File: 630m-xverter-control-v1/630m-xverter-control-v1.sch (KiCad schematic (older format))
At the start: 49 parts, among them J1 Rig Transverter, J2 ALC, J3 ANT, J4 TX_TO_AMP, J5 TX_FROM_AMP, J6 Power, J7 TX AMP POWER, K1 DS1E-M-DC12V, K2 DS1E-M-DC12V, K3 DS1E-M-DC12V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

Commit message: Updates!
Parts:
- added H1, H2, H3, H4: GND, MountingHole:MountingHole_4.3x6.2mm_M4_Pad_Via, symbol Mechanical:MountingHole_Pad
- C1, C2: footprint (none) -> Capacitor_THT:C_Rect_L10.3mm_W5.7mm_P7.50mm_MKS4
- C3: renamed from C1; footprint (none) -> Capacitor_THT:C_Disc_D5.0mm_W2.5mm_P5.00mm
- C4: renamed from C2; footprint (none) -> Capacitor_THT:C_Disc_D5.0mm_W2.5mm_P5.00mm
- C5: renamed from C3; footprint (none) -> Capacitor_THT:C_Disc_D5.0mm_W2.5mm_P5.00mm
- C6: renamed from C4; footprint (none) -> Capacitor_THT:C_Disc_D5.0mm_W2.5mm_P5.00mm
- C7: footprint (none) -> Capacitor_THT:CP_Radial_D10.0mm_P2.50mm
- C8: renamed from C5; footprint (none) -> Capacitor_THT:C_Disc_D5.0mm_W2.5mm_P5.00mm
- C9: renamed from C6; footprint (none) -> Capacitor_THT:CP_Radial_D10.0mm_P2.50mm
- D1, D2: footprint (none) -> Diode_THT:D_DO-35_SOD27_P10.16mm_Horizontal
- D3, D4, D5, D6, D7: footprint (none) -> Diode_THT:D_DO-41_SOD81_P10.16mm_Horizontal
- J1: footprint (none) -> Connector_PinHeader_2.54mm:PinHeader_1x08_P2.54mm_Vertical
- J2, J6, J7: footprint (none) -> Connector_PinHeader_2.54mm:PinHeader_1x02_P2.54mm_Vertical
- J3, J4, J5: footprint (none) -> Connector_Coaxial:SMA_Amphenol_132134-11_Vertical
- K1, K2, K3: footprint Panasonic-DS1E-M-DC12V-0-0-* -> Package_DIP:DIP-12_W7.62mm
- L1, L2, L3: footprint (none) -> coilcraft:coilcraft_slot10
- R1, R10, R2, R3, R4, R5, R6, R7, R8, R9: footprint (none) -> Resistor_THT:R_Axial_DIN0207_L6.3mm_D2.5mm_P7.62mm_Horizontal
- R11: renamed from R9; footprint (none) -> Resistor_THT:R_Axial_DIN0207_L6.3mm_D2.5mm_P7.62mm_Horizontal
- R12: renamed from R10; footprint (none) -> Resistor_THT:R_Axial_DIN0207_L6.3mm_D2.5mm_P7.62mm_Horizontal
- R13: renamed from R11; footprint (none) -> Resistor_THT:R_Axial_DIN0207_L6.3mm_D2.5mm_P10.16mm_Horizontal
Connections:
- net XVERTER_TX_OUTPUT is gone; now on net TX_TO_AMP: J1.7 (Pin_7)
- net GND: now also H1.1, H2.1, H3.1, H4.1

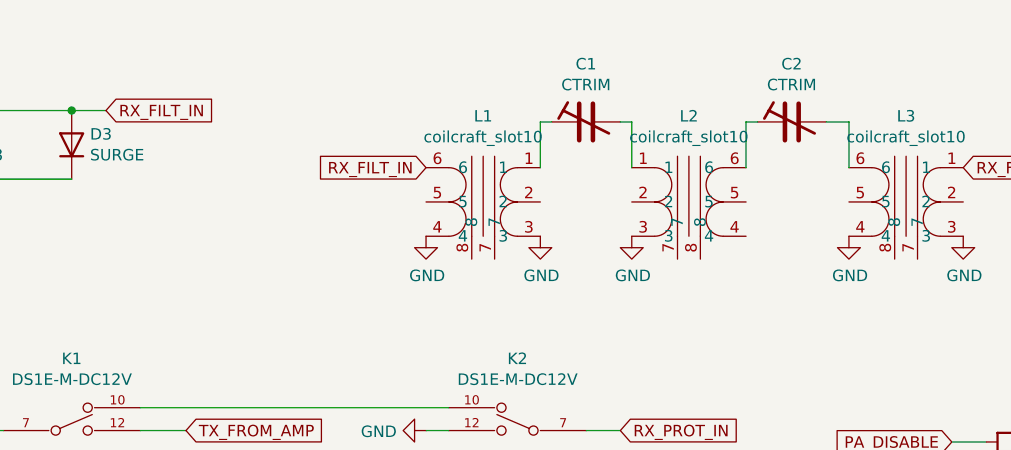
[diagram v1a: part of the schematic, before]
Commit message: Whoops - my coil orientation/pinout was JUST PLAIN WRONG.
So fix the schematic to do the right thing; I'll have to hack something on my
development pcb to test that the filter actually works..
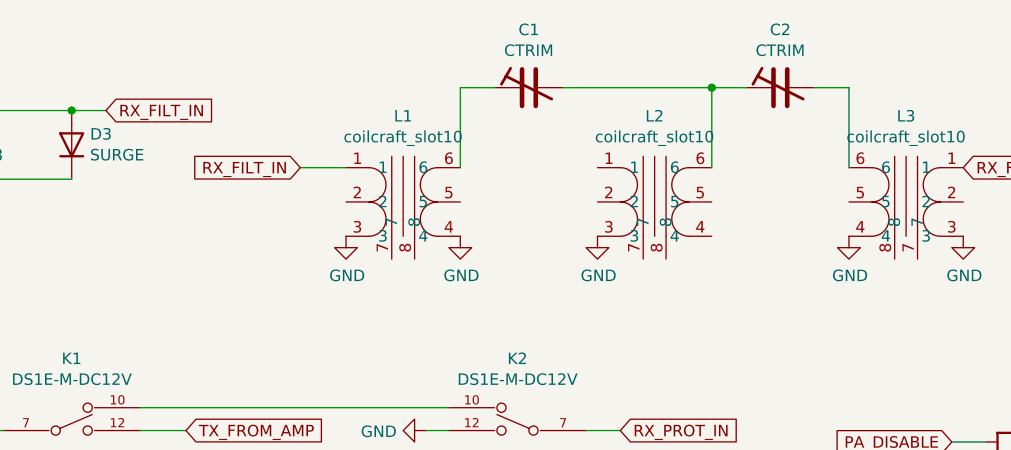
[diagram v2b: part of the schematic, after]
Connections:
- net RX_FILT_IN: now also L1.1; no longer L1.6
- net at C1.1: now also L1.6; no longer L1.1
- net at L2.1: no longer C1.2
- net at C2.1, L2.6: now also C1.2
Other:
- moved on the sheet: C1, C2, L1, L2
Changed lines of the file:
@@
 TX_ENABLE
-$Comp
-L coilcraft:coilcraft_slot10 L1
-U 1 1 5FA3D136
-P 6050 1150
-F 0 "L1" H 6050 1375 50  0000 C CNN
-F 1 "coilcraft_slot10" H 6050 1284 50  0000 C CNN
-F 2 "coilcraft:coilcraft_slot10" H 6050 1150 50  0001 C CNN
-F 3 "" H 6050 1150 50  0001 C CNN
-	1    6050 1150
-	-1   0    0    -1
-$EndComp
 $Comp
 L coilcraft:coilcraft_slot10 L2
 U 1 1 5FA3E025
-P 6950 1150
-F 0 "L2" H 6950 1375 50  0000 C CNN
-F 1 "coilcraft_slot10" H 6950 1284 50  0000 C CNN
-F 2 "coilcraft:coilcraft_slot10" H 6950 1150 50  0001 C CNN
-F 3 "" H 6950 1150 50  0001 C CNN
-	1    6950 1150
+P 6800 1150
+F 0 "L2" H 6800 1375 50  0000 C CNN
+F 1 "coilcraft_slot10" H 6800 1284 50  0000 C CNN
+F 2 "coilcraft:coilcraft_slot10" H 6800 1150 50  0001 C CNN
+F 3 "" H 6800 1150 50  0001 C CNN
+	1    6800 1150
 	1    0    0    -1
 $EndComp
@@
 L power:GND #PWR0103
 U 1 1 5FA420D7
-P 5800 1450
-F 0 "#PWR0103" H 5800 1200 50  0001 C CNN
-F 1 "GND" H 5805 1277 50  0000 C CNN
-F 2 "" H 5800 1450 50  0001 C CNN
-F 3 "" H 5800 1450 50  0001 C CNN
-	1    5800 1450
+P 5450 1450
+F 0 "#PWR0103" H 5450 1200 50  0001 C CNN
+F 1 "GND" H 5455 1277 50  0000 C CNN
+F 2 "" H 5450 1450 50  0001 C CNN
+F 3 "" H 5450 1450 50  0001 C CNN
+	1    5450 1450
 	1    0    0    -1
 $EndComp
@@
 L power:GND #PWR0104
 U 1 1 5FA42988
-P 6300 1450
-F 0 "#PWR0104" H 6300 1200 50  0001 C CNN
-F 1 "GND" H 6305 1277 50  0000 C CNN
-F 2 "" H 6300 1450 50  0001 C CNN
-F 3 "" H 6300 1450 50  0001 C CNN
-	1    6300 1450
+P 5950 1450
+F 0 "#PWR0104" H 5950 1200 50  0001 C CNN
+F 1 "GND" H 5955 1277 50  0000 C CNN
+F 2 "" H 5950 1450 50  0001 C CNN
+F 3 "" H 5950 1450 50  0001 C CNN
+	1    5950 1450
 	1    0    0    -1
 $EndComp
@@
 L power:GND #PWR0105
 U 1 1 5FA47F16
-P 6700 1450
-F 0 "#PWR0105" H 6700 1200 50  0001 C CNN
-F 1 "GND" H 6705 1277 50  0000 C CNN
-F 2 "" H 6700 1450 50  0001 C CNN
-F 3 "" H 6700 1450 50  0001 C CNN
-	1    6700 1450
+P 6550 1450
+F 0 "#PWR0105" H 6550 1200 50  0001 C CNN
+F 1 "GND" H 6555 1277 50  0000 C CNN
+F 2 "" H 6550 1450 50  0001 C CNN
+F 3 "" H 6550 1450 50  0001 C CNN
+	1    6550 1450
 	1    0    0    -1
 $EndComp
@@
 L Device:CTRIM C1
 U 1 1 5FA4943F
-P 6500 950
-F 0 "C1" V 6753 950 50  0000 C CNN
-F 1 "CTRIM" V 6662 950 50  0000 C CNN
-F 2 "Capacitor_THT:C_Rect_L10.3mm_W5.7mm_P7.50mm_MKS4" H 6500 950 50  0001 C CNN
-F 3 "~" H 6500 950 50  0001 C CNN
-	1    6500 950
+P 6250 800
+F 0 "C1" V 6503 800 50  0000 C CNN
+F 1 "CTRIM" V 6412 800 50  0000 C CNN
+F 2 "Capacitor_THT:C_Rect_L10.3mm_W5.7mm_P7.50mm_MKS4" H 6250 800 50  0001 C CNN
+F 3 "~" H 6250 800 50  0001 C CNN
+	1    6250 800
 	0    -1   -1   0
 $EndComp
@@
 L Device:CTRIM C2
 U 1 1 5FA50CBE
-P 7400 950
-F 0 "C2" V 7653 950 50  0000 C CNN
-F 1 "CTRIM" V 7562 950 50  0000 C CNN
-F 2 "Capacitor_THT:C_Rect_L10.3mm_W5.7mm_P7.50mm_MKS4" H 7400 950 50  0001 C CNN
-F 3 "~" H 7400 950 50  0001 C CNN
-	1    7400 950
+P 7350 800
+F 0 "C2" V 7603 800 50  0000 C CNN
+F 1 "CTRIM" V 7512 800 50  0000 C CNN
+F 2 "Capacitor_THT:C_Rect_L10.3mm_W5.7mm_P7.50mm_MKS4" H 7350 800 50  0001 C CNN
+F 3 "~" H 7350 800 50  0001 C CNN
+	1    7350 800
 	0    -1   -1   0
 $EndComp
-Wire Wire Line
-	6350 950  6300 950
-Wire Wire Line
-	6300 950  6300 1150
-Wire Wire Line
-	6650 950  6700 950
-Wire Wire Line
-	6700 950  6700 1150
-Wire Wire Line
-	7250 950  7200 950
-Wire Wire Line
-	7200 950  7200 1150
-Wire Wire Line
-	7550 950  7650 950
-Wire Wire Line
-	7650 950  7650 1150
-Text GLabel 5800 1150 0    50   Input ~ 0
+Text GLabel 5250 1150 0    50   Input ~ 0
 RX_FILT_IN
 Text GLabel 8150 1150 2    50   Input ~ 0
@@
 Wire Wire Line
 	8200 3200 8100 3200
+$Comp
+L coilcraft:coilcraft_slot10 L1
+U 1 1 5FA3D136
+P 5700 1150
+F 0 "L1" H 5700 1375 50  0000 C CNN
+F 1 "coilcraft_slot10" H 5700 1284 50  0000 C CNN
+F 2 "coilcraft:coilcraft_slot10" H 5700 1150 50  0001 C CNN
+F 3 "" H 5700 1150 50  0001 C CNN
+	1    5700 1150
+	1    0    0    -1
+$EndComp
+Wire Wire Line
+	5450 1150 5250 1150
+Wire Wire Line
+	5950 1150 5950 800
+Wire Wire Line
+	5950 800  6100 800
+Wire Wire Line
+	7500 800  7650 800
+Wire Wire Line
+	7650 800  7650 1150
+Wire Wire Line
+	6400 800  7050 800
+Wire Wire Line
+	7050 1150 7050 800
+Connection ~ 7050 800
+Wire Wire Line
+	7050 800  7200 800
 $EndSCHEMATC

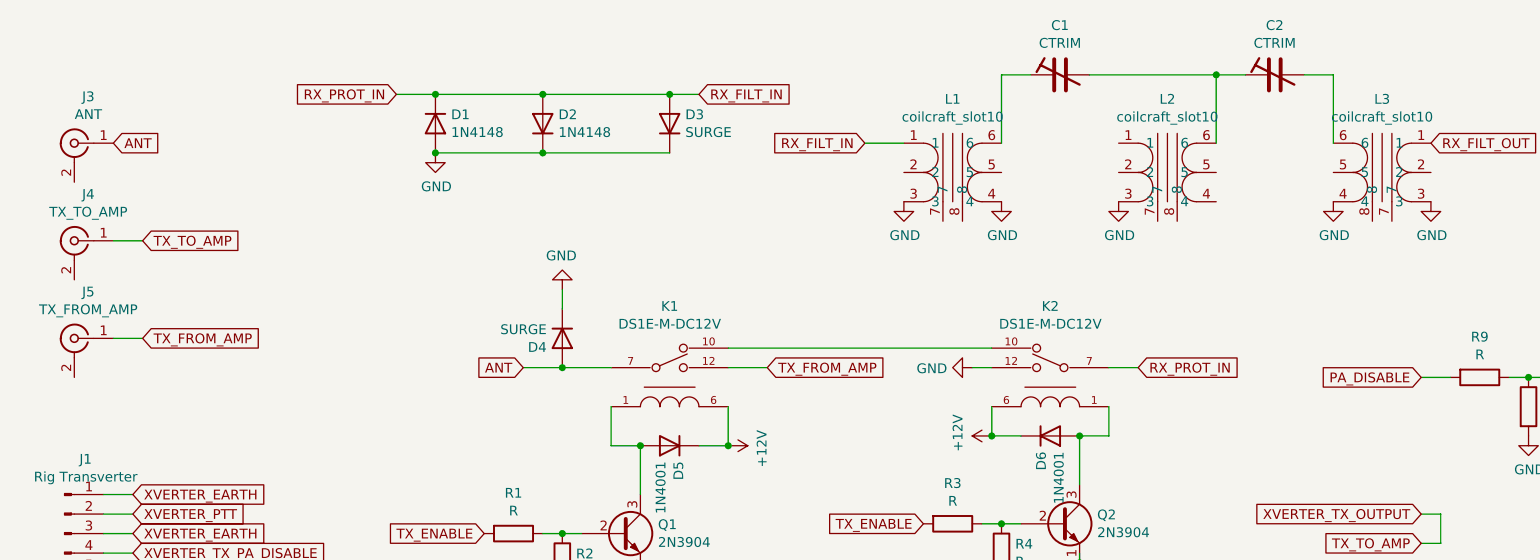
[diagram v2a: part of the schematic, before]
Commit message: more fixes:
* missed ground plane ties for the signal connectors, whoops
* add ground pins for the coils so they can be tied to ground
* add label
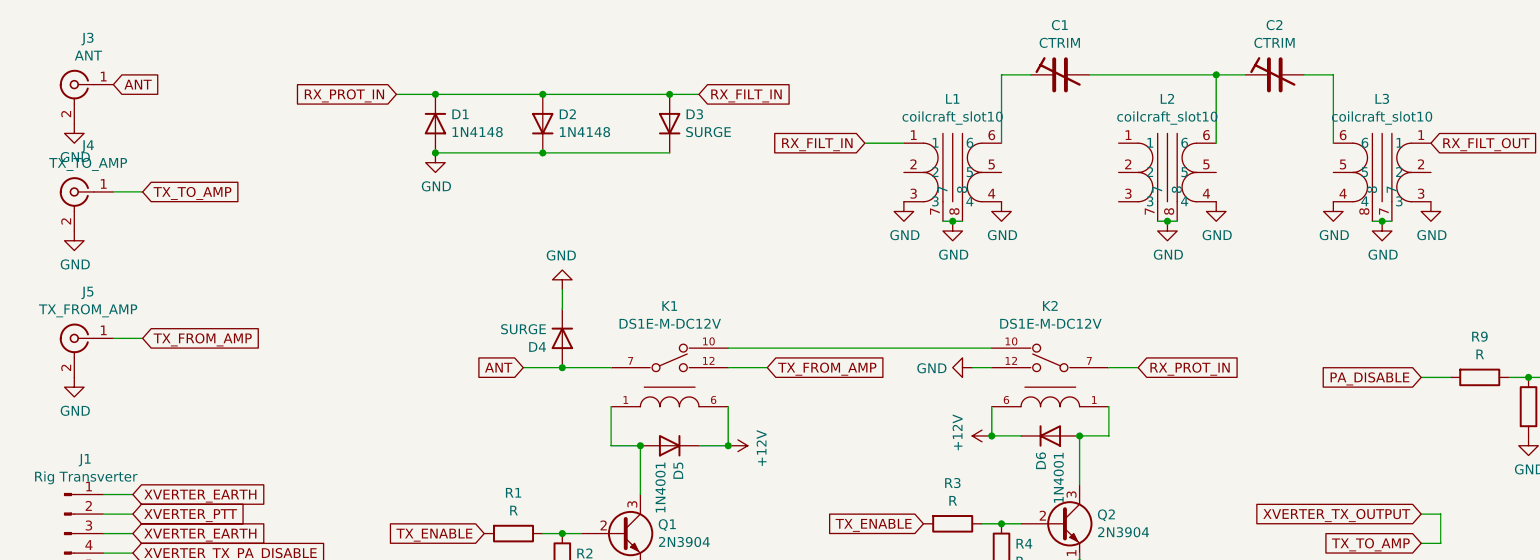
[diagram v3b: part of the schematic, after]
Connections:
- net GND: now also J3.2 (Ext), J4.2 (Ext), J5.2 (Ext), L1.7, L1.8, L2.4, L2.7, L2.8, L3.7, L3.8; no longer L2.3
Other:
- moved on the sheet: J3, J4
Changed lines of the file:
@@
 L power:GND #PWR0105
 U 1 1 5FA47F16
-P 6550 1450
-F 0 "#PWR0105" H 6550 1200 50  0001 C CNN
-F 1 "GND" H 6555 1277 50  0000 C CNN
-F 2 "" H 6550 1450 50  0001 C CNN
-F 3 "" H 6550 1450 50  0001 C CNN
-	1    6550 1450
+P 7050 1450
+F 0 "#PWR0105" H 7050 1200 50  0001 C CNN
+F 1 "GND" H 7055 1277 50  0000 C CNN
+F 2 "" H 7050 1450 50  0001 C CNN
+F 3 "" H 7050 1450 50  0001 C CNN
+	1    7050 1450
 	1    0    0    -1
 $EndComp
@@
 L Connector:Conn_Coaxial J3
 U 1 1 5FA5CD9A
-P 1200 1150
-F 0 "J3" H 1128 1388 50  0000 C CNN
-F 1 "ANT" H 1128 1297 50  0000 C CNN
-F 2 "Connector_Coaxial:SMA_Amphenol_132134-11_Vertical" H 1200 1150 50  0001 C CNN
-F 3 " ~" H 1200 1150 50  0001 C CNN
-	1    1200 1150
+P 1200 850
+F 0 "J3" H 1128 1088 50  0000 C CNN
+F 1 "ANT" H 1128 997 50  0000 C CNN
+F 2 "Connector_Coaxial:SMA_Amphenol_132134-11_Vertical" H 1200 850 50  0001 C CNN
+F 3 " ~" H 1200 850 50  0001 C CNN
+	1    1200 850
 	-1   0    0    -1
 $EndComp
@@
 L Connector:Conn_Coaxial J4
 U 1 1 5FA62FA9
-P 1200 1650
-F 0 "J4" H 1128 1888 50  0000 C CNN
-F 1 "TX_TO_AMP" H 1128 1797 50  0000 C CNN
-F 2 "Connector_Coaxial:SMA_Amphenol_132134-11_Vertical" H 1200 1650 50  0001 C CNN
-F 3 " ~" H 1200 1650 50  0001 C CNN
-	1    1200 1650
+P 1200 1400
+F 0 "J4" H 1128 1638 50  0000 C CNN
+F 1 "TX_TO_AMP" H 1128 1547 50  0000 C CNN
+F 2 "Connector_Coaxial:SMA_Amphenol_132134-11_Vertical" H 1200 1400 50  0001 C CNN
+F 3 " ~" H 1200 1400 50  0001 C CNN
+	1    1200 1400
 	-1   0    0    -1
 $EndComp
@@
 	4400 900  4250 900
 Connection ~ 4250 900
-Text GLabel 1400 1150 2    50   Input ~ 0
+Text GLabel 1400 850  2    50   Input ~ 0
 ANT
 Text GLabel 1500 2950 2    50   Input ~ 0
@@
 Wire Wire Line
 	1350 3650 1500 3650
-Text GLabel 1550 1650 2    50   Input ~ 0
+Text GLabel 1550 1400 2    50   Input ~ 0
 TX_TO_AMP
 Text GLabel 1550 2150 2    50   Input ~ 0
 TX_FROM_AMP
 Wire Wire Line
-	1550 1650 1400 1650
+	1550 1400 1400 1400
 Wire Wire Line
 	1550 2150 1400 2150
@@
 Wire Wire Line
 	7050 800  7200 800
+$Comp
+L power:GND #PWR?
+U 1 1 5FEED7B2
+P 1200 1050
+F 0 "#PWR?" H 1200 800 50  0001 C CNN
+F 1 "GND" H 1205 877 50  0000 C CNN
+F 2 "" H 1200 1050 50  0001 C CNN
+F 3 "" H 1200 1050 50  0001 C CNN
+	1    1200 1050
+	1    0    0    -1
+$EndComp
+$Comp
+L power:GND #PWR?
+U 1 1 5FEF2BFC
+P 1200 1600
+F 0 "#PWR?" H 1200 1350 50  0001 C CNN
+F 1 "GND" H 1205 1427 50  0000 C CNN
+F 2 "" H 1200 1600 50  0001 C CNN
+F 3 "" H 1200 1600 50  0001 C CNN
+	1    1200 1600
+	1    0    0    -1
+$EndComp
+$Comp
+L power:GND #PWR?
+U 1 1 5FEF3573
+P 1200 2350
+F 0 "#PWR?" H 1200 2100 50  0001 C CNN
+F 1 "GND" H 1205 2177 50  0000 C CNN
+F 2 "" H 1200 2350 50  0001 C CNN
+F 3 "" H 1200 2350 50  0001 C CNN
+	1    1200 2350
+	1    0    0    -1
+$EndComp
+Wire Wire Line
+	7850 1550 7900 1550
+Wire Wire Line
+	6750 1550 6800 1550
+Wire Wire Line
+	5650 1550 5700 1550
+$Comp
+L power:GND #PWR?
+U 1 1 5FF0781A
+P 5700 1550
+F 0 "#PWR?" H 5700 1300 50  0001 C CNN
+F 1 "GND" H 5705 1377 50  0000 C CNN
+F 2 "" H 5700 1550 50  0001 C CNN
+F 3 "" H 5700 1550 50  0001 C CNN
+	1    5700 1550
+	1    0    0    -1
+$EndComp
+Connection ~ 5700 1550
+Wire Wire Line
+	5700 1550 5750 1550
+$Comp
+L power:GND #PWR?
+U 1 1 5FF07F9B
+P 6800 1550
+F 0 "#PWR?" H 6800 1300 50  0001 C CNN
+F 1 "GND" H 6805 1377 50  0000 C CNN
+F 2 "" H 6800 1550 50  0001 C CNN
+F 3 "" H 6800 1550 50  0001 C CNN
+	1    6800 1550
+	1    0    0    -1
+$EndComp
+Connection ~ 6800 1550
+Wire Wire Line
+	6800 1550 6850 1550
+$Comp
+L power:GND #PWR?
+U 1 1 5FF08852
+P 7900 1550
+F 0 "#PWR?" H 7900 1300 50  0001 C CNN
+F 1 "GND" H 7905 1377 50  0000 C CNN
+F 2 "" H 7900 1550 50  0001 C CNN
+F 3 "" H 7900 1550 50  0001 C CNN
+	1    7900 1550
+	1    0    0    -1
+$EndComp
+Connection ~ 7900 1550
+Wire Wire Line
+	7900 1550 7950 1550
 $EndSCHEMATC

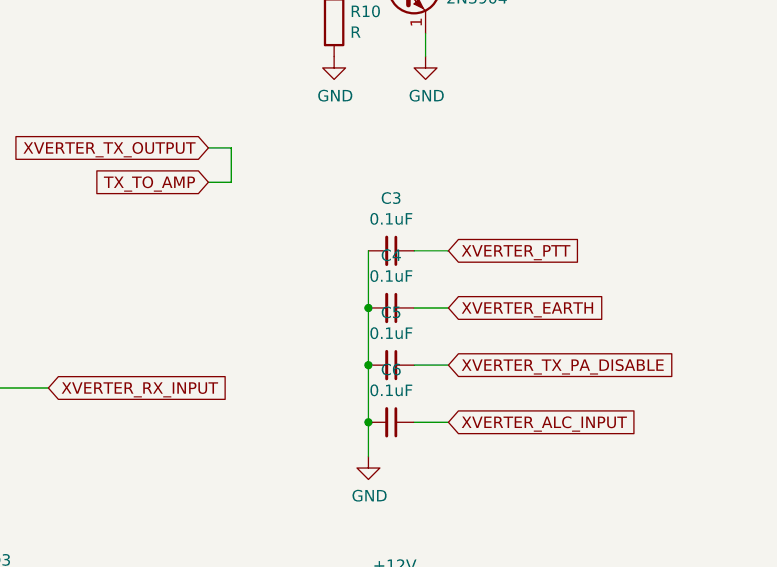
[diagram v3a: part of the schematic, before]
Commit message: More v0.3 fixes -
* fix the bloody signal routing for that middle IF coil, what was I thinking
* don't use a cap to xverter-gnd; just tie them together and to ground

That should be much better!
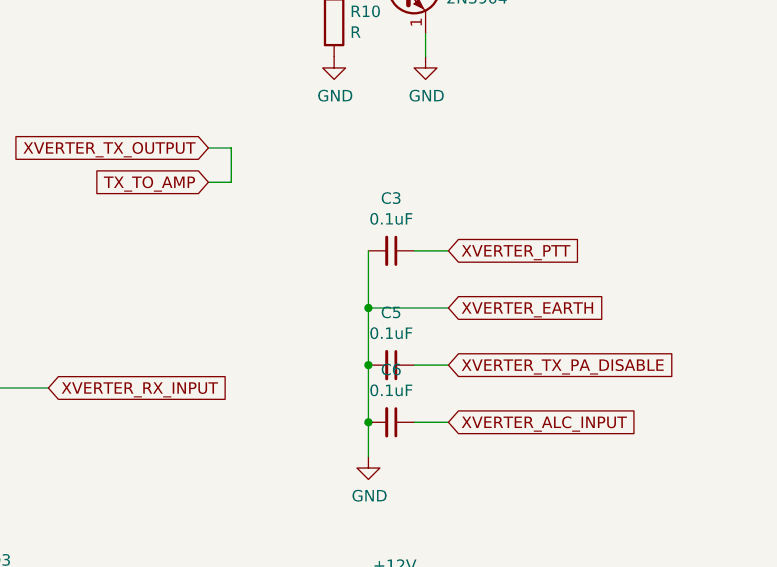
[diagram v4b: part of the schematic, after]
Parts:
- removed C4: 0.1uF, Capacitor_THT:C_Disc_D5.0mm_W2.5mm_P5.00mm, symbol Device:C_Small
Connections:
- net XVERTER_EARTH is gone; now on net GND: J1.1 (Pin_1), J1.3 (Pin_3)
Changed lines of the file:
@@
-$EndComp
-$Comp
-L Device:C_Small C4
-U 1 1 5FCC0258
-P 8900 3750
-F 0 "C4" V 8671 3750 50  0000 C CNN
-F 1 "0.1uF" V 8762 3750 50  0000 C CNN
-F 2 "Capacitor_THT:C_Disc_D5.0mm_W2.5mm_P5.00mm" H 8900 3750 50  0001 C CNN
-F 3 "~" H 8900 3750 50  0001 C CNN
-	1    8900 3750
-	0    1    1    0
 $EndComp
 $Comp
@@
 	1    0    0    -1
 $EndComp
-Wire Wire Line
-	8800 3500 8800 3750
-Connection ~ 8800 3750
-Wire Wire Line
-	8800 3750 8800 4000
 Connection ~ 8800 4000
 Wire Wire Line
@@
 Wire Wire Line
 	9000 3500 9150 3500
-Wire Wire Line
-	9000 3750 9150 3750
 Wire Wire Line
 	9000 4000 9150 4000
@@
 Wire Wire Line
 	7900 1550 7950 1550
+Wire Wire Line
+	8800 3500 8800 3750
+Wire Wire Line
+	9150 3750 8800 3750
+Connection ~ 8800 3750
+Wire Wire Line
+	8800 3750 8800 4000
 $EndSCHEMATC
